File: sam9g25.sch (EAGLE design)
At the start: 131 parts, among them IC1 AT91SAM9G25, IC3 LAN8710, IC4 NCP1529, IC5 NCP1529, IC6 NCP1529, IC7 H5PSXG63JFR, Q1 12MHz, X2 USB-A-HU, X3 MICRO-SD_MOLEX-502774-001, X4 HFJ11-2450E

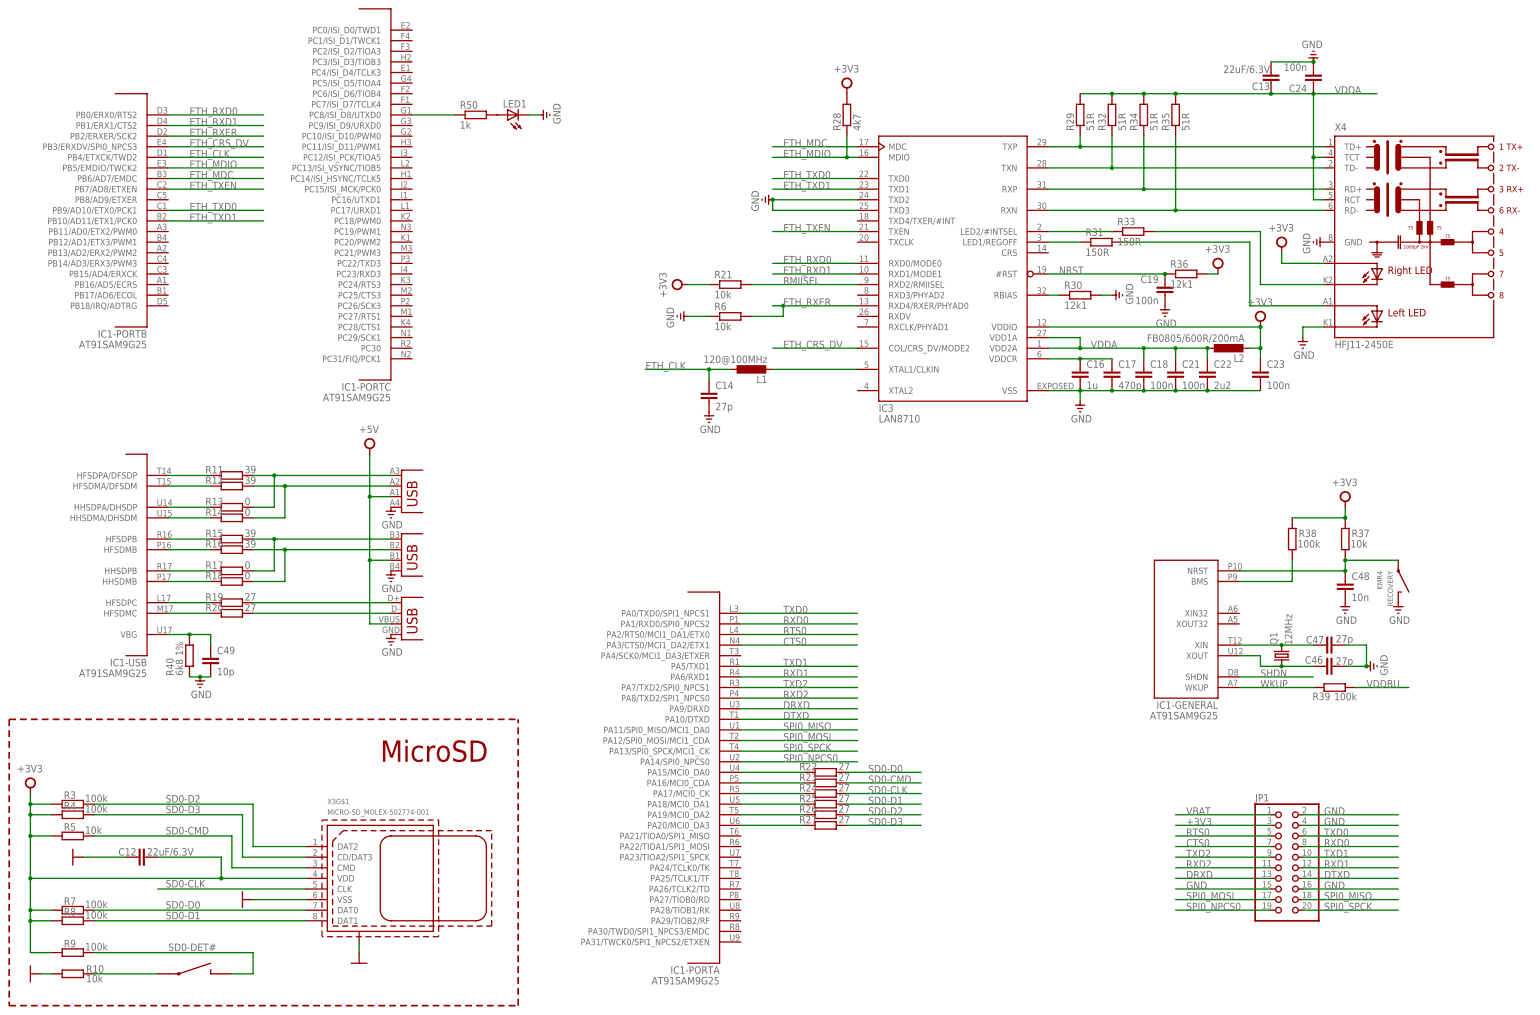
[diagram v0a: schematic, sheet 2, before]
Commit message: Fixed ethernet refclk hardware bug Fixed usb ports
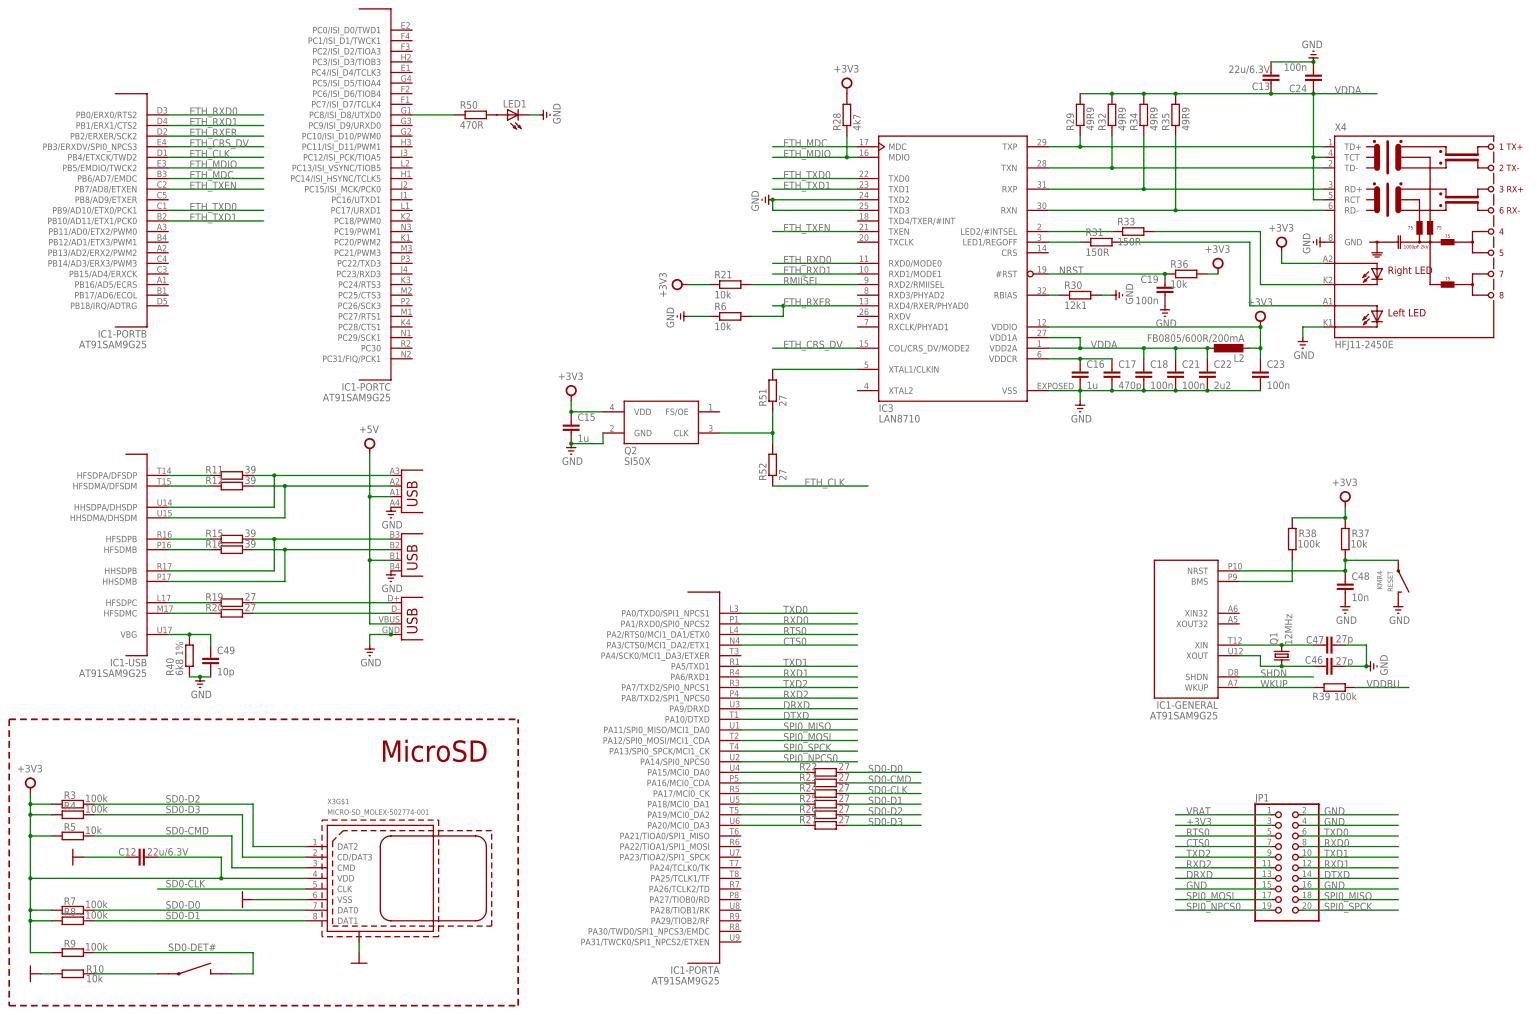
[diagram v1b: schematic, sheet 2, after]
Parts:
- removed C14: 27p, rcl:C-EUC0603
- removed L1: 120@100MHz, mystuff:L-0603
- removed R14, R17, R18: 0, rcl:R-EU_R0603
- removed X2: USB-A-HU, mystuff:USB-A-HU
- added C15: 1u, rcl:C-EUC0603
- added PWR: (no value), led:LEDCHIP-LED0603
- added Q2: SI50X, myrf:SI50X
- added R51, R52: 27, rcl:R-EU_R0603
- added X5: USB-A-HU, mycon:USB-A-HU
- C12, C13: value 22uF/6.3V -> 22u/6.3V
- C50, C53, C56: value 10u/6V3 -> 22u/6V3
- R1, R2: value 1k5 -> 1k
- R13: value 0 -> 1k; MF PANASONIC -> MULTICOMP; MPN ERJ3GEY0R00V -> MCMR06X1001FTL; OC_FARNELL 2059527 -> 2073348
- R29, R32, R34, R35: value 51R -> 49R9
- R36: value 12k1 -> 10k
- R50: value 1k -> 470R
- renumbered RECOVERY to RESET
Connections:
- net N$10 renamed HFSDMB
- net N$15 renamed HFSDPC
- net N$16 renamed HFSDMC
- net N$3 renamed HFSDPA
- net N$4 renamed HFSDMA
- net N$9 renamed HFSDPB
- removed net N$11: R15.2, R17.2, X1-B.D+
- removed net N$12: R16.2, R18.2, X1-B.D-
- removed net N$13: IC1-USB.HHSDPB, R17.1
- removed net N$14: IC1-USB.HHSDMB, R18.1
- removed net N$5: IC1-USB.HHSDPA/DHSDP, R13.1
- removed net N$6: IC1-USB.HHSDMA/DHSDM, R14.1
- removed net N$7: R11.2, R13.2, X1-A.D+
- removed net N$8: R12.2, R14.2, X1-A.D-
- new net HHSDMA: IC1-USB.HHSDMA/DHSDM, R12.2, X1-A.D-
- new net HHSDMB: IC1-USB.HHSDMB, R16.2, X1-B.D-
- new net HHSDPA: IC1-USB.HHSDPA/DHSDP, R11.2, X1-A.D+
- new net HHSDPB: IC1-USB.HHSDPB, R15.2, X1-B.D+
- new net N$4: PWR.A, R13.2
- new net N$46: Q2.CLK, R51.1, R52.2
- net +3V3: now also C15.1, Q2.VDD, R13.1
- net +5V: now also X5.VBUS; no longer X2.VBUS
- net ETH_CLK: now also R52.1; no longer C14.1, L1.1
- net GND: now also C15.2, PWR.C, Q2.GND, X5.GND; no longer C14.2, X2.GND
- net N$17: now also X5.D+; no longer X2.D+
- net N$18: now also X5.D-; no longer X2.D-
- net N$2: now also R51.2; no longer L1.2
